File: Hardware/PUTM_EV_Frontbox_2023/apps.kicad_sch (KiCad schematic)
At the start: 10 parts, among them U8 TLV9152IDDFR

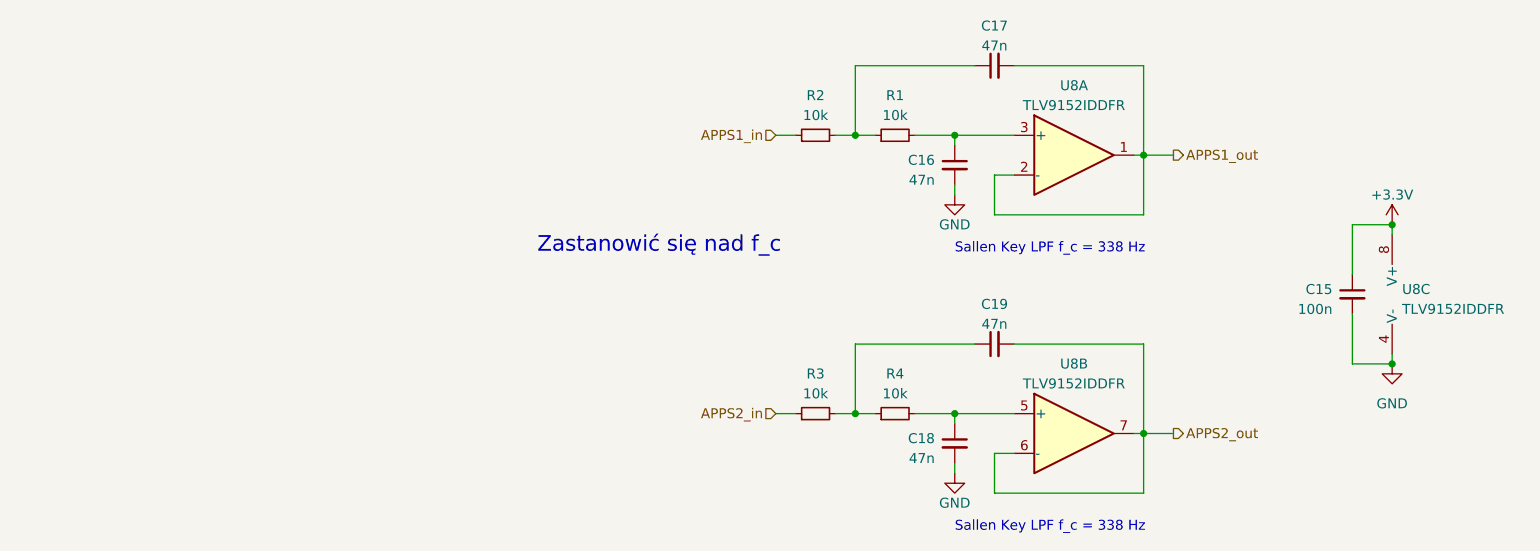
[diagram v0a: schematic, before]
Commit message: Added MCU wiring
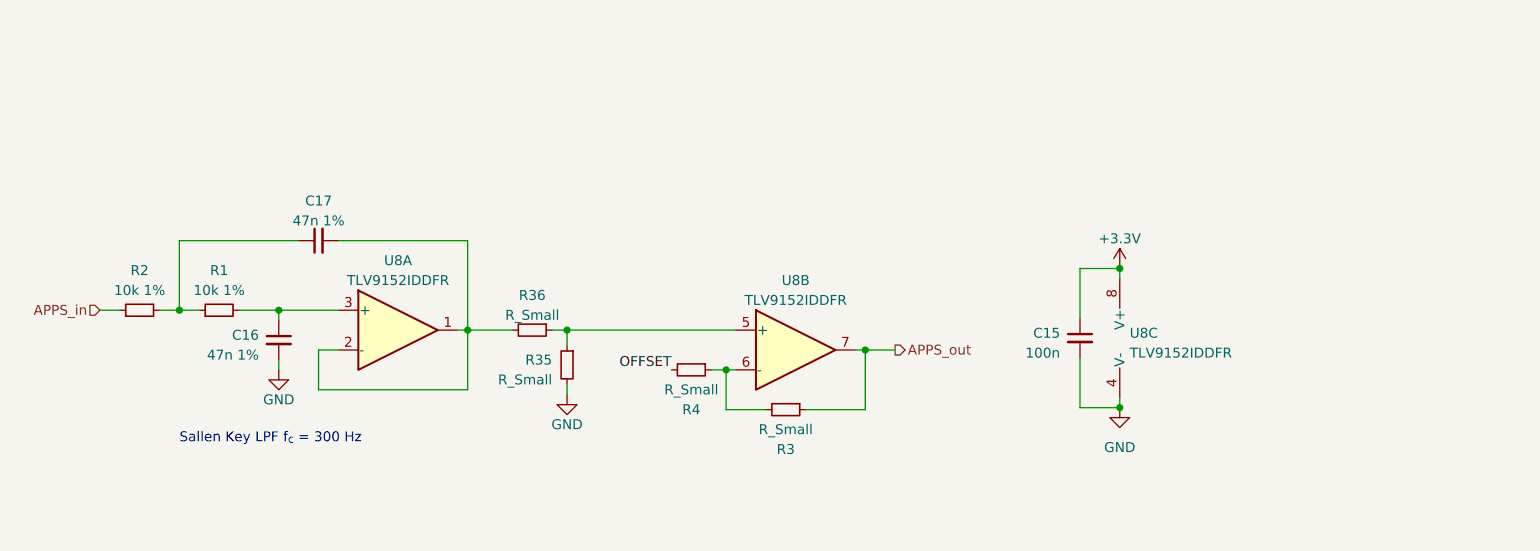
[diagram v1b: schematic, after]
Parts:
- removed C18, C19: 47n, symbol Device:C_Small
- added R35, R36: R_Small, symbol Device:R_Small
- C16, C17: value 47n -> 47n 1%
- R1, R2: value 10k -> 10k 1%
- R3, R4: value 10k -> R_Small
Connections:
- net GND: now also R35.2
- net at U8.5 (+): now also R35.1, R36.1; no longer R4.2
- net at R3.2, R4.1: now also U8.6 (-)
- net APPS1_in renamed APPS_in
- net APPS1_out: no longer names the net of C17.2, U8.1, U8.2 (-)
- net APPS1_out: now also R36.2
- net APPS2_in renamed APPS_out
- net APPS_out: now also U8.7
- removed net APPS2_out: U8.6 (-), U8.7
- new net OFFSET: R4.2
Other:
- note added: "Sallen Key LPF f_{c} = 300 Hz"
- note removed: "Sallen Key LPF f_c = 338 Hz"
- note removed: "Zastanowić się nad f_c"
- title: (none) -> APPS
- moved on the sheet: C15, C16, C17, R1, R2, U8A, U8B, U8C

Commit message: Schematic ready for review
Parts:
- added R30, R31: R_Small, symbol Device:R_Small
- renumbered C16 to C26, C17 to C27, C15 to C28, R2 to R32, R1 to R33, R36 to R34, R4 to R36, R3 to R37, U8 to U13
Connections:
- net GND: now also R31.2
- net OFFSET: now also R30.2, R31.1
- new net +5V: R30.1
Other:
- note added: "Values TBD after selecting potentiometers"
- moved on the sheet: C26, C27, C28, R32, R33, R34, R35, R36, R37, U13A, U13B, U13C

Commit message: Fixed all issues
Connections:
- net +5V renamed 5v_ref
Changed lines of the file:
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@@
     (effects (font (size 1.27 1.27)) (justify left bottom))
+  )
+  (global_label "5v_ref" (shape input) (at 29.21 95.885 0) (fields_autoplaced)
+    (effects (font (size 1.27 1.27)) (justify left))
+    (property "Intersheetrefs" "${INTERSHEET_REFS}" (at 37.861 95.885 0)
+      (effects (font (size 1.27 1.27)) (justify left) hide)
+    )
   )
   (hierarchical_label "APPS_in" (shape input) (at 51.435 101.6 180) (fields_autoplaced)
@@
         )
       )
-    )
-  )
-  (symbol (lib_id "power:+5V") (at 29.21 95.885 0) (mirror y) (unit 1)
-    (in_bom yes) (on_board yes) (dnp no) (fields_autoplaced)
-    (property "Reference" "#PWR095" (at 29.21 99.695 0)
-      (effects (font (size 1.27 1.27)) hide)
-    )
-    (property "Value" "+5V" (at 29.21 92.075 0)
-      (effects (font (size 1.27 1.27)))
-    )
-    (property "Footprint" "" (at 29.21 95.885 0)
-      (effects (font (size 1.27 1.27)) hide)
-    )
-    (property "Datasheet" "" (at 29.21 95.885 0)
-      (effects (font (size 1.27 1.27)) hide)
-    )
-    (pin "1")
-    (instances
-      (project "PUTM_EV_Frontbox_2023"
-        (path "/b652b05a-4e3d-4ad1-b032-18886abe7d45/55cf8599-7fcf-4ad3-afe8-d836ab083f74"
-          (reference "#PWR095") (unit 1)
-        )
-        (path "/b652b05a-4e3d-4ad1-b032-18886abe7d45/89069515-a409-433b-9ed0-2772e97aaa2d"
-          (reference "#PWR092") (unit 1)
-        )
-        (path "/b652b05a-4e3d-4ad1-b032-18886abe7d45/de50c137-74f9-4e43-93cb-58ddb34925e1"
-          (reference "#PWR0110") (unit 1)
-        )
-        (path "/b652b05a-4e3d-4ad1-b032-18886abe7d45/92e1c237-4df1-4ea5-b062-79b6d493fbfe"
-          (reference "#PWR0120") (unit 1)
-        )
-      )

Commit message: Schematic modified, footprints assigned
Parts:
- C26, C27, C28: footprint (none) -> Capacitor_SMD:C_0402_1005Metric_Pad0.74x0.62mm_HandSolder
- R30, R31, R32, R33, R34, R35, R36, R37: footprint (none) -> Resistor_SMD:R_0402_1005Metric
- U13: footprint (none) -> Package_TO_SOT_SMD:TSOT-23-8_HandSoldering
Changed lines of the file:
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@@
           (reference "#PWR093") (unit 1)
         )
-        (path "/b652b05a-4e3d-4ad1-b032-18886abe7d45/de50c137-74f9-4e43-93cb-58ddb34925e1"
-          (reference "#PWR0111") (unit 1)
-        )
         (path "/b652b05a-4e3d-4ad1-b032-18886abe7d45/92e1c237-4df1-4ea5-b062-79b6d493fbfe"
           (reference "#PWR0121") (unit 1)
@@
       (effects (font (size 1.27 1.27)))
     )
-    (property "Footprint" "" (at 139.065 114.3 0)
+    (property "Footprint" "Resistor_SMD:R_0402_1005Metric" (at 139.065 114.3 0)
       (effects (font (size 1.27 1.27)) hide)
     )
@@
           (reference "R74") (unit 1)
         )
-        (path "/b652b05a-4e3d-4ad1-b032-18886abe7d45/de50c137-74f9-4e43-93cb-58ddb34925e1"
-          (reference "R65") (unit 1)
-        )
       )
     )
@@
       (effects (font (size 1.27 1.27)))
     )
-    (property "Footprint" "" (at 106.68 104.14 0)
+    (property "Footprint" "Resistor_SMD:R_0402_1005Metric" (at 106.68 104.14 0)
       (effects (font (size 1.27 1.27)) hide)
     )
@@
           (reference "R71") (unit 1)
         )
-        (path "/b652b05a-4e3d-4ad1-b032-18886abe7d45/de50c137-74f9-4e43-93cb-58ddb34925e1"
-          (reference "R62") (unit 1)
-        )
       )
     )
@@
           (reference "#PWR0125") (unit 1)
         )
-        (path "/b652b05a-4e3d-4ad1-b032-18886abe7d45/de50c137-74f9-4e43-93cb-58ddb34925e1"
-          (reference "#PWR0115") (unit 1)
-        )
       )
     )
@@
       (effects (font (size 1.27 1.27)) (justify left))
     )
-    (property "Footprint" "" (at 182.88 104.775 0)
+    (property "Footprint" "Package_TO_SOT_SMD:TSOT-23-8_HandSoldering" (at 182.88 104.775 0)
       (effects (font (size 1.27 1.27)) hide)
     )
@@
           (reference "U18") (unit 3)
         )
-        (path "/b652b05a-4e3d-4ad1-b032-18886abe7d45/de50c137-74f9-4e43-93cb-58ddb34925e1"
-          (reference "U16") (unit 3)
-        )
       )
     )
@@
       (effects (font (size 1.27 1.27)))
     )
-    (property "Footprint" "" (at 56.515 101.6 0)
+    (property "Footprint" "Resistor_SMD:R_0402_1005Metric" (at 56.515 101.6 0)
       (effects (font (size 1.27 1.27)) hide)
     )
@@
           (reference "R69") (unit 1)
         )
-        (path "/b652b05a-4e3d-4ad1-b032-18886abe7d45/de50c137-74f9-4e43-93cb-58ddb34925e1"
-          (reference "R60") (unit 1)
-        )
       )
     )
@@
       (effects (font (size 1.27 1.27)) (justify left))
     )
-    (property "Footprint" "" (at 29.21 99.695 0)
+    (property "Footprint" "Resistor_SMD:R_0402_1005Metric" (at 29.21 99.695 0)
       (effects (font (size 1.27 1.27)) hide)
     )
@@
           (reference "R30") (unit 1)
         )
-        (path "/b652b05a-4e3d-4ad1-b032-18886abe7d45/de50c137-74f9-4e43-93cb-58ddb34925e1"
-          (reference "R58") (unit 1)
-        )
         (path "/b652b05a-4e3d-4ad1-b032-18886abe7d45/92e1c237-4df1-4ea5-b062-79b6d493fbfe"
           (reference "R67") (unit 1)
@@
           (reference "#PWR0124") (unit 1)
         )
-        (path "/b652b05a-4e3d-4ad1-b032-18886abe7d45/de50c137-74f9-4e43-93cb-58ddb34925e1"
-          (reference "#PWR0114") (unit 1)
-        )
       )
     )
@@
       (effects (font (size 1.27 1.27)) (justify left))
     )
-    (property "Footprint" "" (at 29.21 107.315 0)
+    (property "Footprint" "Resistor_SMD:R_0402_1005Metric" (at 29.21 107.315 0)
       (effects (font (size 1.27 1.27)) hide)
     )
@@
           (reference "R31") (unit 1)
         )
-        (path "/b652b05a-4e3d-4ad1-b032-18886abe7d45/de50c137-74f9-4e43-93cb-58ddb34925e1"
-          (reference "R59") (unit 1)
-        )
         (path "/b652b05a-4e3d-4ad1-b032-18886abe7d45/92e1c237-4df1-4ea5-b062-79b6d493fbfe"
           (reference "R68") (unit 1)
@@
       (effects (font (size 1.27 1.27)))
     )
-    (property "Footprint" "" (at 127 109.22 0)
+    (property "Footprint" "Resistor_SMD:R_0402_1005Metric" (at 127 109.22 0)
       (effects (font (size 1.27 1.27)) hide)
     )
@@
           (reference "R73") (unit 1)
         )
-        (path "/b652b05a-4e3d-4ad1-b032-18886abe7d45/de50c137-74f9-4e43-93cb-58ddb34925e1"
-          (reference "R64") (unit 1)
-        )
       )
     )
@@
       (effects (font (size 1.27 1.27)))
     )
-    (property "Footprint" "" (at 140.335 106.68 0)
+    (property "Footprint" "Package_TO_SOT_SMD:TSOT-23-8_HandSoldering" (at 140.335 106.68 0)
       (effects (font (size 1.27 1.27)) hide)
     )
@@
           (reference "U18") (unit 2)
         )
-        (path "/b652b05a-4e3d-4ad1-b032-18886abe7d45/de50c137-74f9-4e43-93cb-58ddb34925e1"
-          (reference "U16") (unit 2)
-        )
       )
     )
@@
           (reference "#PWR0123") (unit 1)
         )
-        (path "/b652b05a-4e3d-4ad1-b032-18886abe7d45/de50c137-74f9-4e43-93cb-58ddb34925e1"
-          (reference "#PWR0113") (unit 1)
-        )
       )
     )
@@
         (path "/b652b05a-4e3d-4ad1-b032-18886abe7d45/92e1c237-4df1-4ea5-b062-79b6d493fbfe"
           (reference "#PWR0122") (unit 1)
-        )
-        (path "/b652b05a-4e3d-4ad1-b032-18886abe7d45/de50c137-74f9-4e43-93cb-58ddb34925e1"
-          (reference "#PWR0112") (unit 1)
         )
       )
@@
       (effects (font (size 1.27 1.27)) (justify right))
     )
-    (property "Footprint" "" (at 175.26 104.775 0)
+    (property "Footprint" "Capacitor_SMD:C_0402_1005Metric_Pad0.74x0.62mm_HandSolder" (at 175.26 104.775 0)
       (effects (font (size 1.27 1.27)) hide)
     )
@@
           (reference "C35") (unit 1)
         )
-        (path "/b652b05a-4e3d-4ad1-b032-18886abe7d45/de50c137-74f9-4e43-93cb-58ddb34925e1"
-          (reference "C32") (unit 1)
-        )
       )
     )
@@
       (effects (font (size 1.27 1.27)) (justify left))
     )
-    (property "Footprint" "" (at 111.125 108.585 0)
+    (property "Footprint" "Resistor_SMD:R_0402_1005Metric" (at 111.125 108.585 0)
       (effects (font (size 1.27 1.27)) hide)
     )
@@
           (reference "R72") (unit 1)
         )
-        (path "/b652b05a-4e3d-4ad1-b032-18886abe7d45/de50c137-74f9-4e43-93cb-58ddb34925e1"
-          (reference "R63") (unit 1)
-        )
       )
     )
@@
       (effects (font (size 1.27 1.27)))
     )
-    (property "Footprint" "" (at 79.375 92.71 0)
+    (property "Footprint" "Capacitor_SMD:C_0402_1005Metric_Pad0.74x0.62mm_HandSolder" (at 79.375 92.71 0)
       (effects (font (size 1.27 1.27)) hide)
     )
@@
         (path "/b652b05a-4e3d-4ad1-b032-18886abe7d45/92e1c237-4df1-4ea5-b062-79b6d493fbfe"
           (reference "C34") (unit 1)
-        )
-        (path "/b652b05a-4e3d-4ad1-b032-18886abe7d45/de50c137-74f9-4e43-93cb-58ddb34925e1"
-          (reference "C31") (unit 1)
         )
       )
@@
       (effects (font (size 1.27 1.27)) (justify right))
     )
-    (property "Footprint" "" (at 74.295 105.41 0)
+    (property "Footprint" "Capacitor_SMD:C_0402_1005Metric_Pad0.74x0.62mm_HandSolder" (at 74.295 105.41 0)
       (effects (font (size 1.27 1.27)) hide)
     )
@@
           (reference "C33") (unit 1)
         )
-        (path "/b652b05a-4e3d-4ad1-b032-18886abe7d45/de50c137-74f9-4e43-93cb-58ddb34925e1"
-          (reference "C30") (unit 1)
-        )
       )
     )
@@
       (effects (font (size 1.27 1.27)))
     )
-    (property "Footprint" "" (at 66.675 101.6 0)
+    (property "Footprint" "Resistor_SMD:R_0402_1005Metric" (at 66.675 101.6 0)
       (effects (font (size 1.27 1.27)) hide)
     )
@@
           (reference "R70") (unit 1)
         )
-        (path "/b652b05a-4e3d-4ad1-b032-18886abe7d45/de50c137-74f9-4e43-93cb-58ddb34925e1"
-          (reference "R61") (unit 1)
-        )
       )
     )
@@
       (effects (font (size 1.27 1.27)))
     )
-    (property "Footprint" "" (at 89.535 104.14 0)
+    (property "Footprint" "Package_TO_SOT_SMD:TSOT-23-8_HandSoldering" (at 89.535 104.14 0)
       (effects (font (size 1.27 1.27)) hide)
     )
@@
           (reference "U18") (unit 1)
         )
-        (path "/b652b05a-4e3d-4ad1-b032-18886abe7d45/de50c137-74f9-4e43-93cb-58ddb34925e1"
-          (reference "U16") (unit 1)
-        )
-      )
+      )
